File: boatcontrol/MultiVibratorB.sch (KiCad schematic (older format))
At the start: 5 parts, among them IC401 CD74HCT221E, U302 74HC86

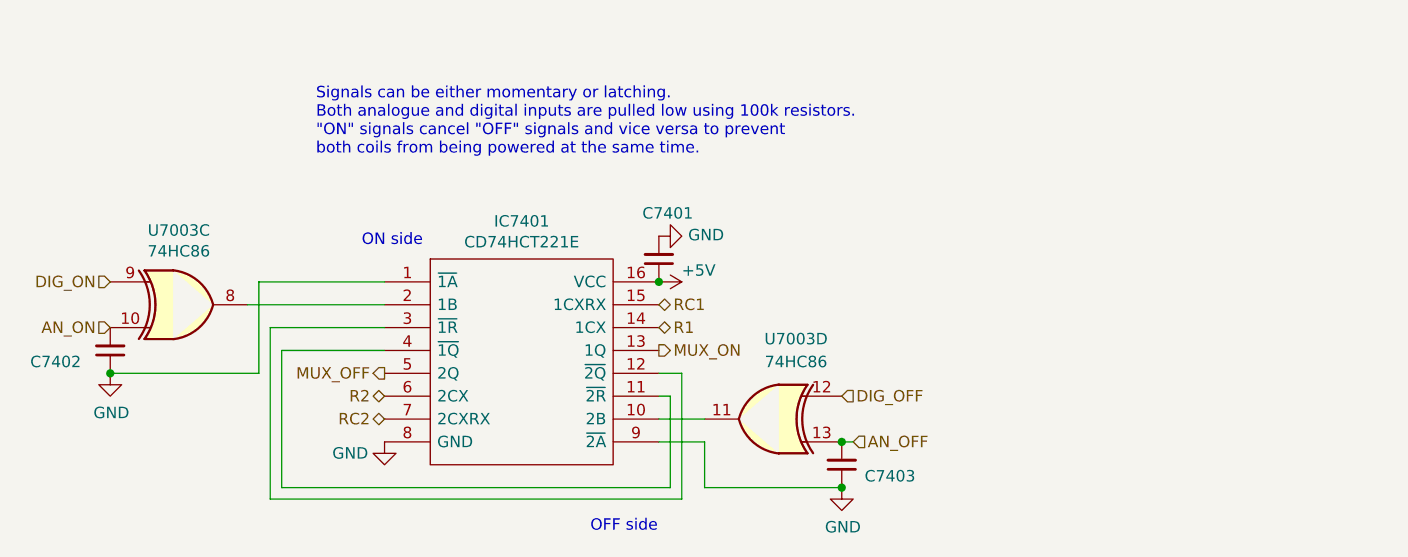
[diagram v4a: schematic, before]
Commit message: Switch to common 5v 10K ohm for an sigs
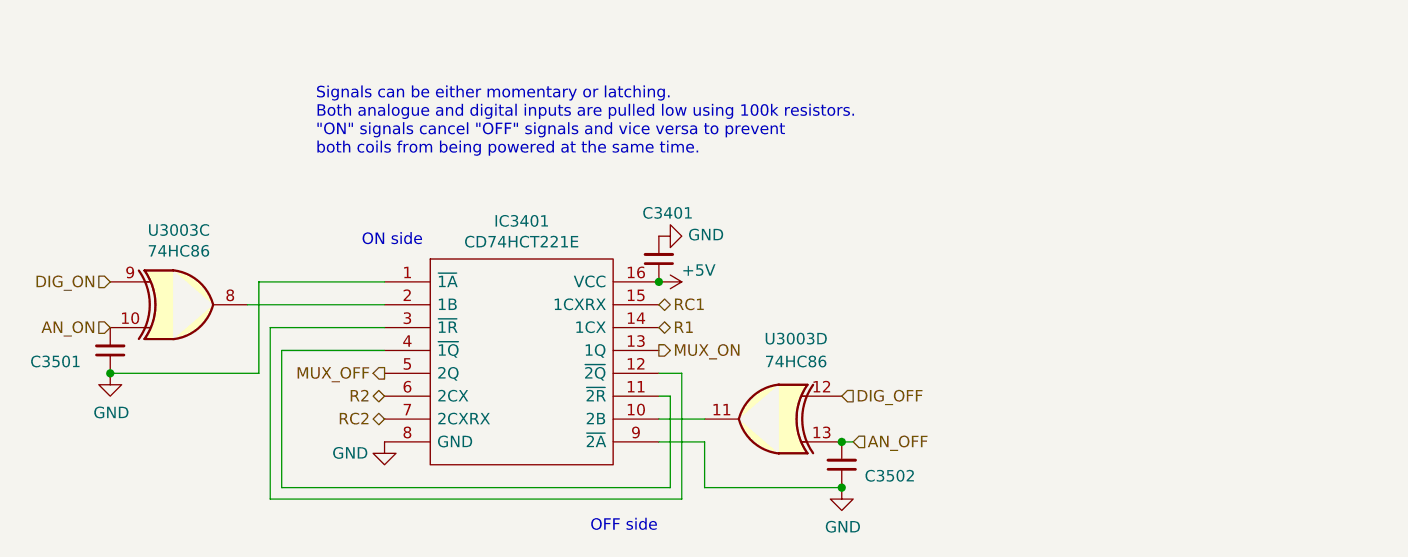
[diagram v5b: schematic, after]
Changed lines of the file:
@@
 $Descr A4 11693 8268
 encoding utf-8
-Sheet 66 97
+Sheet 35 97
 Title "Boat Control Hat"
 Date ""
@@
 AR Path="/D1BB8DB4/5F75E923/604747F3/5FD2B9DE" Ref="IC7301"  Part="1"
 AR Path="/D1BB8DB4/5F75E923/604747FF/5FD2B9DE" Ref="IC7401"  Part="1"
-F 0 "IC7401" H 5450 4215 50  0000 C CNN
+F 0 "IC3401" H 5450 4215 50  0000 C CNN
 F 1 "CD74HCT221E" H 5450 4124 50  0000 C CNN
 F 2 "DIP794W53P254L1930H508Q16N" H 5900 4050 50  0001 L CNN
@@
 AR Path="/D1BB8DB4/5F75E923/604747F3/60314A0F" Ref="#PWR07302"  Part="1"
 AR Path="/D1BB8DB4/5F75E923/604747FF/60314A0F" Ref="#PWR07402"  Part="1"
-F 0 "#PWR07402" H 4850 4400 50  0001 C CNN
+F 0 "#PWR03402" H 4850 4400 50  0001 C CNN
 F 1 "GND" H 4700 4600 50  0000 C CNN
 F 2 "" H 4850 4650 50  0001 C CNN
@@
 AR Path="/D1BB8DB4/5F75E923/604747F3/5FD9FC74" Ref="#PWR07301"  Part="1"
 AR Path="/D1BB8DB4/5F75E923/604747FF/5FD9FC74" Ref="#PWR07401"  Part="1"
-F 0 "#PWR07401" H 6050 3800 50  0001 C CNN
+F 0 "#PWR03401" H 6050 3800 50  0001 C CNN
 F 1 "+5V" V 6000 4050 50  0000 L CNN
 F 2 "" H 6050 3950 50  0001 C CNN
@@
 AR Path="/D1BB8DB4/5F317CB5/60365B0F/61CAF5C8" Ref="#PWR0183"  Part="1"
 AR Path="/D1BB8DB4/5F317CB5/60365B35/61CAF5C8" Ref="#PWR0185"  Part="1"
-F 0 "#PWR0182" H 6050 3500 50  0001 C CNN
+F 0 "#PWR0170" H 6050 3500 50  0001 C CNN
 F 1 "GND" V 6055 3622 50  0000 R CNN
 F 2 "" H 6050 3750 50  0001 C CNN
@@
 AR Path="/D1BB8DB4/5F317CB5/60365B0F/61CAE2AB" Ref="C8001"  Part="1"
 AR Path="/D1BB8DB4/5F317CB5/60365B35/61CAE2AB" Ref="C8201"  Part="1"
-F 0 "C7401" H 5900 3650 50  0000 L CNN
+F 0 "C3401" H 5900 3650 50  0000 L CNN
 F 1 "0.1μF" H 6141 3805 50  0001 L CNN
 F 2 "Capacitor_THT:C_Disc_D7.5mm_W5.0mm_P5.00mm" H 6050 3850 50  0001 C CNN
@@
 AR Path="/D1BB8DB4/5F317CB5/60365B29/602120C6" Ref="C8103"  Part="1"
 AR Path="/D1BB8DB4/5F317CB5/60365B41/602120C6" Ref="C8303"  Part="1"
-F 0 "C7403" H 6950 4800 50  0000 L CNN
+F 0 "C3502" H 6950 4800 50  0000 L CNN
 F 1 "1µF" H 6000 4650 50  0001 L CNN
 F 2 "Capacitor_THT:C_Disc_D7.5mm_W5.0mm_P5.00mm" H 6850 4750 50  0001 C CNN
@@
 AR Path="/D1BB8DB4/5F317CB5/60365B29/60314A11" Ref="#PWR0350"  Part="1"
 AR Path="/D1BB8DB4/5F317CB5/60365B41/60314A11" Ref="#PWR0354"  Part="1"
-F 0 "#PWR0339" H 6850 4600 50  0001 C CNN
+F 0 "#PWR0293" H 6850 4600 50  0001 C CNN
 F 1 "GND" H 6855 4677 50  0000 C CNN
 F 2 "" H 6850 4850 50  0001 C CNN
@@
 AR Path="/D1BB8DB4/5F317CB5/60365B29/60216860" Ref="#PWR0351"  Part="1"
 AR Path="/D1BB8DB4/5F317CB5/60365B41/60216860" Ref="#PWR0355"  Part="1"
-F 0 "#PWR0340" H 3650 4100 50  0001 C CNN
+F 0 "#PWR0294" H 3650 4100 50  0001 C CNN
 F 1 "GND" H 3655 4177 50  0000 C CNN
 F 2 "" H 3650 4350 50  0001 C CNN
@@
 AR Path="/D1BB8DB4/5F317CB5/60365B29/6021685A" Ref="C8102"  Part="1"
 AR Path="/D1BB8DB4/5F317CB5/60365B41/6021685A" Ref="C8302"  Part="1"
-F 0 "C7402" H 3300 4300 50  0000 L CNN
+F 0 "C3501" H 3300 4300 50  0000 L CNN
 F 1 "1µF" H 2800 4150 50  0001 L CNN
 F 2 "Capacitor_THT:C_Disc_D7.5mm_W5.0mm_P5.00mm" H 3650 4250 50  0001 C CNN
@@
 AR Path="/D1BB8DB4/5F317CB5/60365B29/604BDC57" Ref="U7902"  Part="3"
 AR Path="/D1BB8DB4/5F317CB5/60365B41/604BDC57" Ref="U7903"  Part="3"
-F 0 "U7003" H 3950 4375 50  0000 C CNN
+F 0 "U3003" H 3950 4375 50  0000 C CNN
 F 1 "74HC86" H 3950 4284 50  0000 C CNN
 F 2 "" H 3950 4050 50  0001 C CNN
@@
 AR Path="/D1BB8DB4/5F317CB5/60365B29/604BF9DE" Ref="U7902"  Part="4"
 AR Path="/D1BB8DB4/5F317CB5/60365B41/604BF9DE" Ref="U7903"  Part="4"
-F 0 "U7003" H 6450 4900 50  0000 C CNN
+F 0 "U3003" H 6450 4900 50  0000 C CNN
 F 1 "74HC86" H 6450 4800 50  0000 C CNN
 F 2 "" H 6550 4550 50  0001 C CNN

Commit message: Sorted Caps
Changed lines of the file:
@@
 $Descr A4 11693 8268
 encoding utf-8
-Sheet 35 97
+Sheet 44 97
 Title "Boat Control Hat"
 Date ""
@@
 AR Path="/D1BB8DB4/5F75E923/604747F3/5FD2B9DE" Ref="IC7301"  Part="1"
 AR Path="/D1BB8DB4/5F75E923/604747FF/5FD2B9DE" Ref="IC7401"  Part="1"
-F 0 "IC3401" H 5450 4215 50  0000 C CNN
+F 0 "IC5601" H 5450 4215 50  0000 C CNN
 F 1 "CD74HCT221E" H 5450 4124 50  0000 C CNN
 F 2 "DIP794W53P254L1930H508Q16N" H 5900 4050 50  0001 L CNN
@@
 AR Path="/D1BB8DB4/5F75E923/604747F3/60314A0F" Ref="#PWR07302"  Part="1"
 AR Path="/D1BB8DB4/5F75E923/604747FF/60314A0F" Ref="#PWR07402"  Part="1"
-F 0 "#PWR03402" H 4850 4400 50  0001 C CNN
+F 0 "#PWR05602" H 4850 4400 50  0001 C CNN
 F 1 "GND" H 4700 4600 50  0000 C CNN
 F 2 "" H 4850 4650 50  0001 C CNN
@@
 AR Path="/D1BB8DB4/5F75E923/604747F3/5FD9FC74" Ref="#PWR07301"  Part="1"
 AR Path="/D1BB8DB4/5F75E923/604747FF/5FD9FC74" Ref="#PWR07401"  Part="1"
-F 0 "#PWR03401" H 6050 3800 50  0001 C CNN
+F 0 "#PWR05601" H 6050 3800 50  0001 C CNN
 F 1 "+5V" V 6000 4050 50  0000 L CNN
 F 2 "" H 6050 3950 50  0001 C CNN
@@
 AR Path="/D1BB8DB4/5F317CB5/60365B0F/61CAF5C8" Ref="#PWR0183"  Part="1"
 AR Path="/D1BB8DB4/5F317CB5/60365B35/61CAF5C8" Ref="#PWR0185"  Part="1"
-F 0 "#PWR0170" H 6050 3500 50  0001 C CNN
+F 0 "#PWR0174" H 6050 3500 50  0001 C CNN
 F 1 "GND" V 6055 3622 50  0000 R CNN
 F 2 "" H 6050 3750 50  0001 C CNN
@@
 AR Path="/D1BB8DB4/5F317CB5/60365B0F/61CAE2AB" Ref="C8001"  Part="1"
 AR Path="/D1BB8DB4/5F317CB5/60365B35/61CAE2AB" Ref="C8201"  Part="1"
-F 0 "C3401" H 5900 3650 50  0000 L CNN
+F 0 "C5601" H 5900 3650 50  0000 L CNN
 F 1 "0.1μF" H 6141 3805 50  0001 L CNN
 F 2 "Capacitor_THT:C_Disc_D7.5mm_W5.0mm_P5.00mm" H 6050 3850 50  0001 C CNN
@@
 AR Path="/D1BB8DB4/5F317CB5/60365B29/602120C6" Ref="C8103"  Part="1"
 AR Path="/D1BB8DB4/5F317CB5/60365B41/602120C6" Ref="C8303"  Part="1"
-F 0 "C3502" H 6950 4800 50  0000 L CNN
+F 0 "C5603" H 6950 4800 50  0000 L CNN
 F 1 "1µF" H 6000 4650 50  0001 L CNN
 F 2 "Capacitor_THT:C_Disc_D7.5mm_W5.0mm_P5.00mm" H 6850 4750 50  0001 C CNN
@@
 AR Path="/D1BB8DB4/5F317CB5/60365B29/60314A11" Ref="#PWR0350"  Part="1"
 AR Path="/D1BB8DB4/5F317CB5/60365B41/60314A11" Ref="#PWR0354"  Part="1"
-F 0 "#PWR0293" H 6850 4600 50  0001 C CNN
+F 0 "#PWR0317" H 6850 4600 50  0001 C CNN
 F 1 "GND" H 6855 4677 50  0000 C CNN
 F 2 "" H 6850 4850 50  0001 C CNN
@@
 AR Path="/D1BB8DB4/5F317CB5/60365B29/60216860" Ref="#PWR0351"  Part="1"
 AR Path="/D1BB8DB4/5F317CB5/60365B41/60216860" Ref="#PWR0355"  Part="1"
-F 0 "#PWR0294" H 3650 4100 50  0001 C CNN
+F 0 "#PWR0318" H 3650 4100 50  0001 C CNN
 F 1 "GND" H 3655 4177 50  0000 C CNN
 F 2 "" H 3650 4350 50  0001 C CNN
@@
 AR Path="/D1BB8DB4/5F317CB5/60365B29/6021685A" Ref="C8102"  Part="1"
 AR Path="/D1BB8DB4/5F317CB5/60365B41/6021685A" Ref="C8302"  Part="1"
-F 0 "C3501" H 3300 4300 50  0000 L CNN
+F 0 "C5602" H 3300 4300 50  0000 L CNN
 F 1 "1µF" H 2800 4150 50  0001 L CNN
 F 2 "Capacitor_THT:C_Disc_D7.5mm_W5.0mm_P5.00mm" H 3650 4250 50  0001 C CNN
@@
 AR Path="/D1BB8DB4/5F317CB5/60365B29/604BDC57" Ref="U7902"  Part="3"
 AR Path="/D1BB8DB4/5F317CB5/60365B41/604BDC57" Ref="U7903"  Part="3"
-F 0 "U3003" H 3950 4375 50  0000 C CNN
+F 0 "U4003" H 3950 4375 50  0000 C CNN
 F 1 "74HC86" H 3950 4284 50  0000 C CNN
 F 2 "" H 3950 4050 50  0001 C CNN
@@
 AR Path="/D1BB8DB4/5F317CB5/60365B29/604BF9DE" Ref="U7902"  Part="4"
 AR Path="/D1BB8DB4/5F317CB5/60365B41/604BF9DE" Ref="U7903"  Part="4"
-F 0 "U3003" H 6450 4900 50  0000 C CNN
+F 0 "U4003" H 6450 4900 50  0000 C CNN
 F 1 "74HC86" H 6450 4800 50  0000 C CNN
 F 2 "" H 6550 4550 50  0001 C CNN
